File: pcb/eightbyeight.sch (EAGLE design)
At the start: 139 parts, among them CON1 USB_MICROSMT+THRUHULE, Q1 16MHz, SW1 SWITCH_SPDT, SW2 BRIGHTNESS, U1 MK20DN64VFM5, U10 FDG6316P, U11 FDG6316P, U12 FDG6316P, U2 ICN2026, U3 74138, U4 ICN2026, U5 MIC5219 3.3V, U6 ESP_WROOM_02, U8 MMA8653FC, U9 FDG6316P

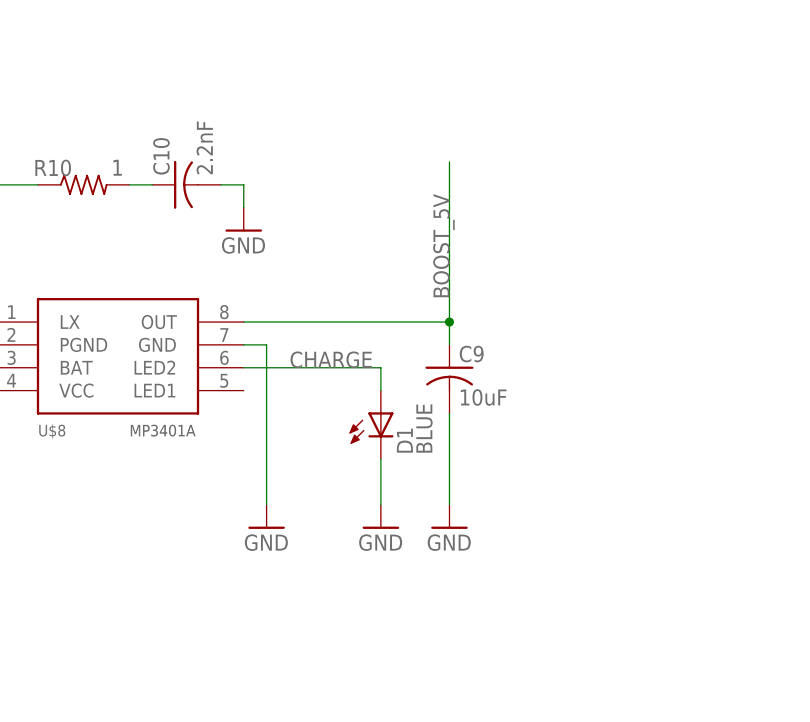
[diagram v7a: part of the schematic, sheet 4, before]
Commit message: Add discharge LED, finish board routing!
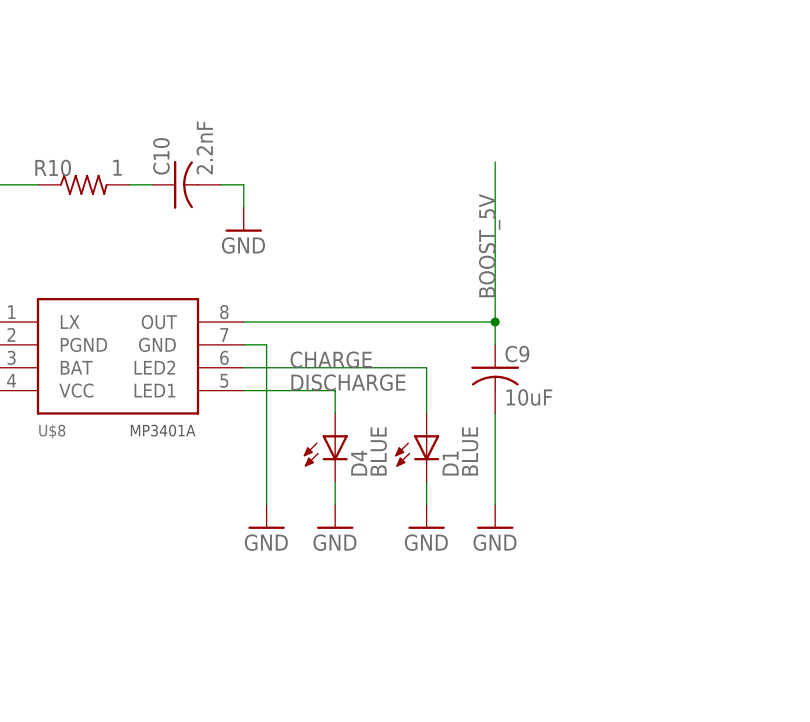
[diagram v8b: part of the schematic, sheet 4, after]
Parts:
- added D4: BLUE, adafruit:LEDCHIP-LED0603
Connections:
- new net DISCHARGE: D4.A, U$8.LED1
- net GND: now also D4.C
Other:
- moved on the sheet: C9, D1
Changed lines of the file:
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@@
 <part name="3V7" library="supply1" deviceset="+3V3" device=""/>
 <part name="GND44" library="supply1" deviceset="GND" device=""/>
+<part name="D4" library="adafruit" deviceset="LED" device="CHIP-LED0603" value="BLUE"/>
+<part name="GND45" library="SparkFun-Aesthetics" deviceset="GND" device=""/>
 </parts>
 <sheets>
@@
 <instance part="GND12" gate="1" x="109.22" y="187.96"/>
 <instance part="P+13" gate="1" x="63.5" y="129.54"/>
-<instance part="GND15" gate="1" x="129.54" y="187.96"/>
-<instance part="D1" gate="G$1" x="121.92" y="200.66"/>
-<instance part="GND20" gate="1" x="121.92" y="187.96"/>
+<instance part="GND15" gate="1" x="134.62" y="187.96"/>
+<instance part="D1" gate="G$1" x="127" y="198.12"/>
+<instance part="GND20" gate="1" x="127" y="187.96"/>
 <instance part="GND36" gate="1" x="45.72" y="187.96"/>
 <instance part="R10" gate="G$1" x="88.9" y="226.06" smashed="yes">
@@
 <instance part="C10" gate="G$1" x="99.06" y="226.06" rot="R90"/>
 <instance part="C12" gate="G$1" x="45.72" y="198.12"/>
-<instance part="C9" gate="G$1" x="129.54" y="205.74"/>
+<instance part="C9" gate="G$1" x="134.62" y="205.74"/>
 <instance part="C6" gate="G$1" x="248.92" y="205.74"/>
 <instance part="GND38" gate="1" x="248.92" y="195.58"/>
@@
 <instance part="R11" gate="G$1" x="48.26" y="99.06" rot="R90"/>
 <instance part="GND43" gate="1" x="48.26" y="86.36"/>
+<instance part="D4" gate="G$1" x="116.84" y="198.12"/>
+<instance part="GND45" gate="1" x="116.84" y="187.96"/>
 </instances>
 <busses>
@@
 </segment>
 <segment>
-<wire x1="129.54" y1="200.66" x2="129.54" y2="190.5" width="0.1524" layer="91"/>
+<wire x1="134.62" y1="200.66" x2="134.62" y2="190.5" width="0.1524" layer="91"/>
 <pinref part="GND15" gate="1" pin="GND"/>
 <pinref part="C9" gate="G$1" pin="2"/>
@@
 <pinref part="GND20" gate="1" pin="GND"/>
 <pinref part="D1" gate="G$1" pin="C"/>
-<wire x1="121.92" y1="190.5" x2="121.92" y2="195.58" width="0.1524" layer="91"/>
+<wire x1="127" y1="190.5" x2="127" y2="193.04" width="0.1524" layer="91"/>
 </segment>
 <segment>
@@
 <wire x1="48.26" y1="93.98" x2="48.26" y2="88.9" width="0.1524" layer="91"/>
 <pinref part="GND43" gate="1" pin="GND"/>
+</segment>
+<segment>
+<pinref part="D4" gate="G$1" pin="C"/>
+<wire x1="116.84" y1="193.04" x2="116.84" y2="190.5" width="0.1524" layer="91"/>
+<pinref part="GND45" gate="1" pin="GND"/>
 </segment>
 </net>
@@
 <pinref part="U$8" gate="G$1" pin="LED2"/>
 <pinref part="D1" gate="G$1" pin="A"/>
-<wire x1="106.68" y1="205.74" x2="121.92" y2="205.74" width="0.1524" layer="91"/>
-<wire x1="121.92" y1="205.74" x2="121.92" y2="203.2" width="0.1524" layer="91"/>
+<wire x1="106.68" y1="205.74" x2="127" y2="205.74" width="0.1524" layer="91"/>
+<wire x1="127" y1="205.74" x2="127" y2="200.66" width="0.1524" layer="91"/>
 <label x="111.76" y="205.74" size="1.778" layer="95"/>
 </segment>
@@
 <segment>
 <pinref part="U$8" gate="G$1" pin="OUT"/>
-<wire x1="106.68" y1="210.82" x2="129.54" y2="210.82" width="0.1524" layer="91"/>
-<wire x1="129.54" y1="210.82" x2="129.54" y2="208.28" width="0.1524" layer="91"/>
+<wire x1="106.68" y1="210.82" x2="134.62" y2="210.82" width="0.1524" layer="91"/>
+<wire x1="134.62" y1="210.82" x2="134.62" y2="208.28" width="0.1524" layer="91"/>
 <pinref part="C9" gate="G$1" pin="1"/>
-<label x="129.54" y="213.36" size="1.778" layer="95" rot="R90"/>
-<wire x1="129.54" y1="210.82" x2="129.54" y2="228.6" width="0.1524" layer="91"/>
-<junction x="129.54" y="210.82"/>
+<label x="134.62" y="213.36" size="1.778" layer="95" rot="R90"/>
+<wire x1="134.62" y1="210.82" x2="134.62" y2="228.6" width="0.1524" layer="91"/>
+<junction x="134.62" y="210.82"/>
 </segment>
 <segment>
@@
 </segment>
 </net>
+<net name="DISCHARGE" class="0">
+<segment>
+<pinref part="U$8" gate="G$1" pin="LED1"/>
+<pinref part="D4" gate="G$1" pin="A"/>
+<wire x1="106.68" y1="203.2" x2="116.84" y2="203.2" width="0.1524" layer="91"/>
+<wire x1="116.84" y1="203.2" x2="116.84" y2="200.66" width="0.1524" layer="91"/>
+<label x="111.76" y="203.2" size="1.778" layer="95"/>
+</segment>
+</net>
